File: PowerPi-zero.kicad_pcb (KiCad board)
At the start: 2 copper layers, 65 x 56 mm, 34 parts, among them J1 2444, J3 Conn_01x02, J6 Raspberry_Pi_2_3, J8 2444, Q1 30V 4A 44mΩ, Q2 50nA 150V 200mW 200mA, Q3 30V 4A 44mΩ, U1 XL4015

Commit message: Layout complete for PowerPi zero
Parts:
- removed D2: SS54, Diode_SMD:D_SMA
- removed H5, H6, H7, H8: MountingHole, MountingHole:MountingHole_3.5mm
- removed J3: Conn_01x02, Connector_JST:JST_XH_B2B-XH-A_1x02_P2.50mm_Vertical
- removed JP1: SolderJumper_3_Bridged12, Jumper:SolderJumper-3_P1.3mm_Bridged2Bar12_RoundedPad1.0x1.5mm
- moved R1 46.0 mm to (121.0, 107.1), turned to 180 degrees
- moved Q2 45.7 mm to (123.7, 106.4)
- moved R2 44.7 mm to (122.7, 100.7), turned to 0 degrees
- moved C1 44.0 mm to (104.2, 117.4), turned to 180 degrees
- moved Q3 43.9 mm to (123.6, 103.1), turned to 0 degrees
- moved R8 43.6 mm to (151.8, 115.4), turned to 180 degrees
- moved R6 42.2 mm to (151.8, 111.3), turned to 180 degrees
- moved D5 41.8 mm to (153.6, 114.6), turned to -90 degrees
- moved D3 41.0 mm to (153.6, 110.5), turned to -90 degrees
- moved H2 40.5 mm to (93.2, 97.0)
- moved H3 40.5 mm to (151.2, 97.0)
- moved J6 40.5 mm to (98.1, 98.3)
- moved J8 38.1 mm to (151.5, 102.8), turned to -90 degrees
- moved C2 37.0 mm to (111.4, 121.3), turned to -90 degrees
- moved C3 36.4 mm to (111.4, 118.1), turned to -90 degrees
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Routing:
- net VCC: track 29.0 -> 40.9 mm, vias 3 -> 0
- net Net-(D2-Pad1): track 8.10 -> 0.00 mm, vias 1 -> 0
- net +5V: track 2.95 -> 9.34 mm, vias 1 -> 0
- net Net-(D6-Pad1): track 22.4 -> 26.8 mm
- net Net-(Q2-Pad3): track 5.83 -> 7.27 mm
- net Net-(R10-Pad1): track 12.0 -> 12.7 mm
- net GND: track 4.99 -> 5.08 mm, vias 56 -> 50
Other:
- board size 65 x 56 mm -> 65 x 30 mm
- board text added: "Select one of these board edges depending upon the type of socket that is used."
- board text removed: "+"
- board text removed: "-"
- board text removed: "."
- board text removed: "12/24V"
- board text removed: "5V"
- board text removed: "AUX 5V(1A)"
- board text removed: "FAN"
- board text removed: "JLCJLCJLC"
- board text removed: "VCC"
- board text removed: "Vector 3D PowerPi Designed by Sreenivas Eadara"

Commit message: cleanup
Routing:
- net Net-(D6-Pad1): track 26.8 -> 26.1 mm
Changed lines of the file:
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@@
     (style (thickness 0.15) (arrow_length 1.27) (text_position_mode 0) (extension_height 0.58642) (extension_offset 0) keep_text_aligned)
   )
-  (segment (start 151.29 115.4) (end 151.29 115.41) (width 0.5) (layer "F.Cu") (net 1))
   (segment (start 151.29 115.41) (end 143.9 122.8) (width 0.5) (layer "F.Cu") (net 1))
   (segment (start 143.9 122.8) (end 113.45 122.8) (width 0.5) (layer "F.Cu") (net 1))
@@
   (via (at 119.8 107.1) (size 0.6) (drill 0.4) (layers "F.Cu" "B.Cu") (net 2))
   (segment (start 111.4 117.325) (end 114.9 117.325) (width 1) (layer "F.Cu") (net 3))
-  (segment (start 114.9 117.325) (end 114.925 117.3) (width 1) (layer "F.Cu") (net 3))
   (segment (start 151.280001 111.3) (end 149.5 109.519999) (width 0.5) (layer "F.Cu") (net 4))
   (segment (start 149.5 109.519999) (end 149.5 102.7) (width 0.5) (layer "F.Cu") (net 4))
-  (segment (start 153.5875 111.3) (end 153.6 111.2875) (width 0.5) (layer "F.Cu") (net 5))
   (segment (start 152.300001 111.3) (end 153.5875 111.3) (width 0.5) (layer "F.Cu") (net 5))
-  (segment (start 153.5875 115.4) (end 153.6 115.3875) (width 0.5) (layer "F.Cu") (net 6))
   (segment (start 152.31 115.4) (end 153.5875 115.4) (width 0.5) (layer "F.Cu") (net 6))
-  (segment (start 139.55 120.75) (end 139.1 120.3) (width 2) (layer "F.Cu") (net 7))
   (segment (start 128.375 119.9) (end 124.075 115.6) (width 2) (layer "F.Cu") (net 7))
   (segment (start 131.25 120.3) (end 131 120.05) (width 2) (layer "F.Cu") (net 7))
@@
   (segment (start 139.1 120.3) (end 131.25 120.3) (width 2) (layer "F.Cu") (net 7))
   (segment (start 122.75 107.05) (end 121.56 107.05) (width 0.375) (layer "F.Cu") (net 31))
-  (segment (start 121.56 107.05) (end 121.51 107.1) (width 0.375) (layer "F.Cu") (net 31))
   (segment (start 122.75 106.4) (end 124.65 106.4) (width 0.375) (layer "F.Cu") (net 31))
   (segment (start 122.75 107.05) (end 122.75 106.4) (width 0.375) (layer "F.Cu") (net 31))

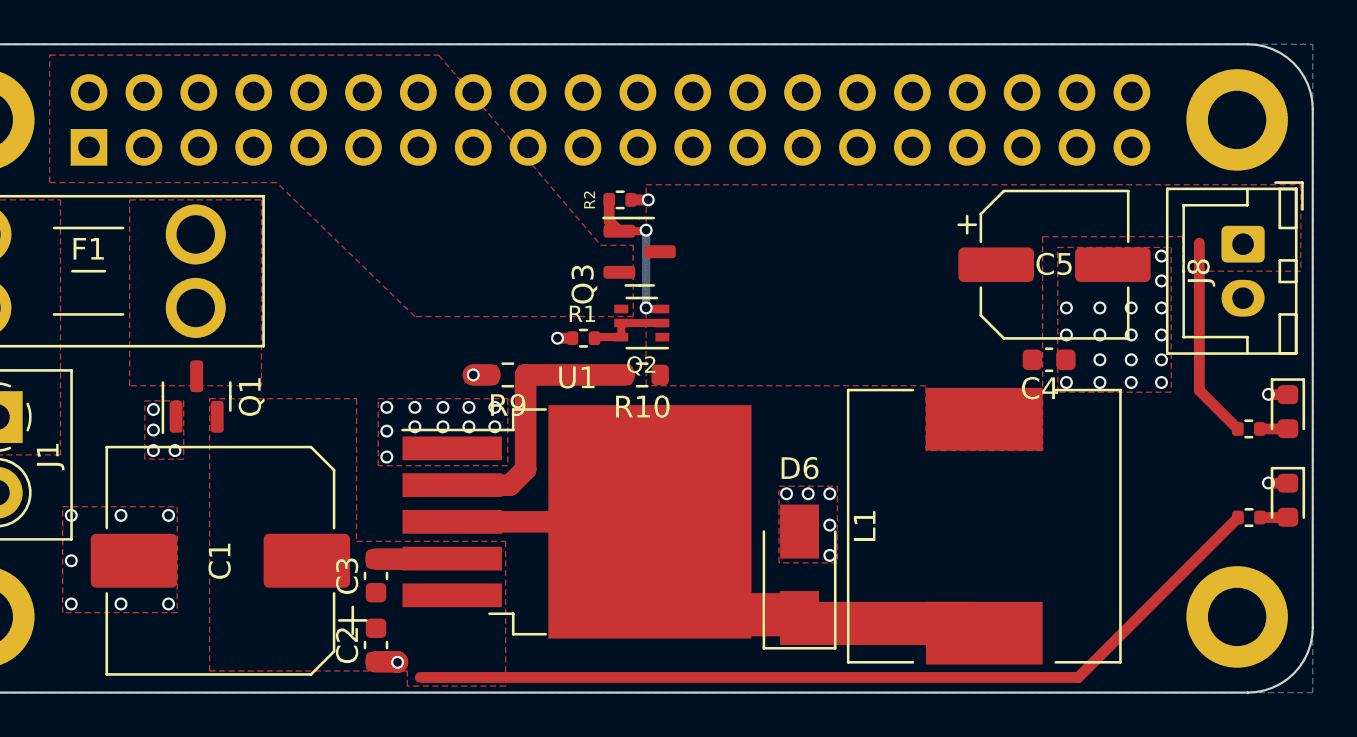
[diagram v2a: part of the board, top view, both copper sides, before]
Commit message: updated layout
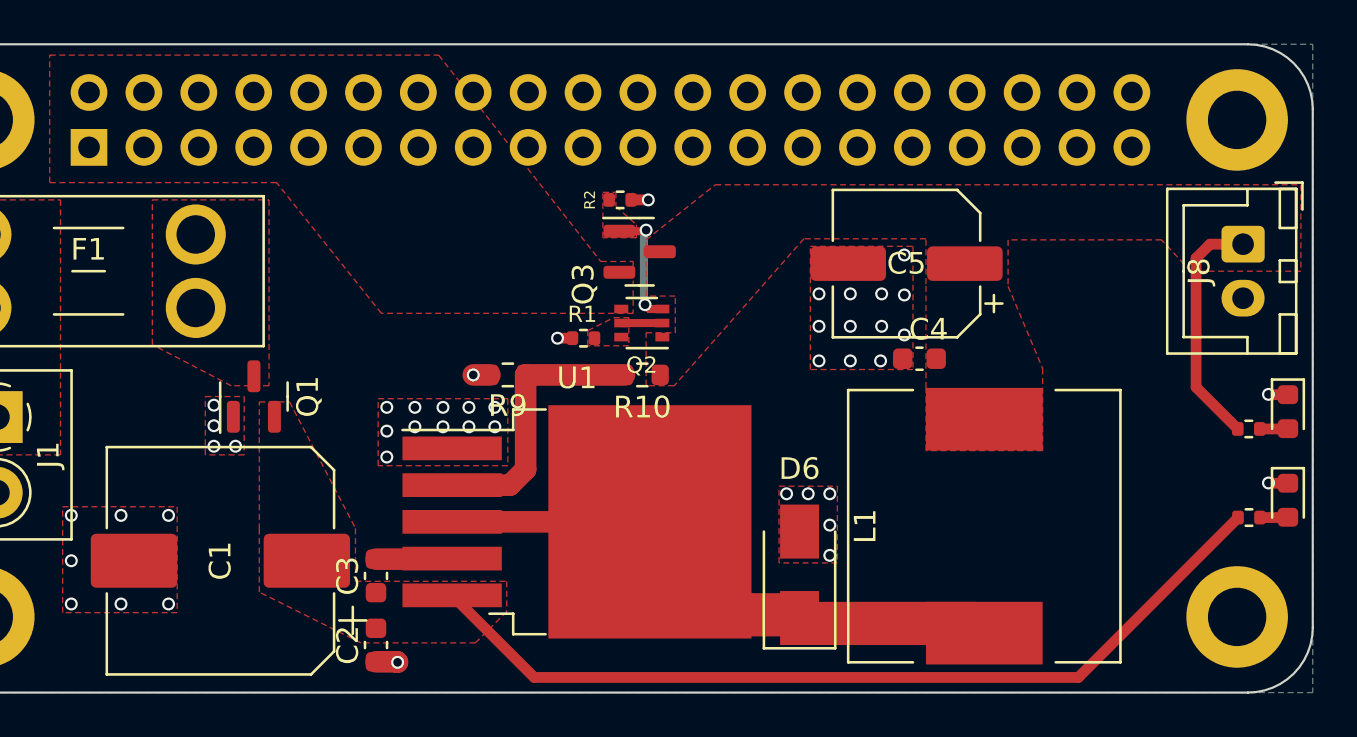
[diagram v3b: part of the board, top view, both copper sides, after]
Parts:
- moved C5 6.85 mm to (135.9, 103.7), turned to 180 degrees
- moved C4 6.00 mm to (136.6, 108.0), turned to 180 degrees
- moved Q1 2.65 mm to (105.8, 109.8)
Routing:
- net +5V: track 9.34 -> 11.2 mm
- net Net-(Q2-Pad2): track 3.74 -> 1.90 mm
- net Net-(Q2-Pad3): track 7.27 -> 5.65 mm
- net GND: vias 50 -> 45
- added copper zone on F.Cu, net Net-(Q2-Pad2)
- added copper zone on F.Cu, net Net-(Q2-Pad3)

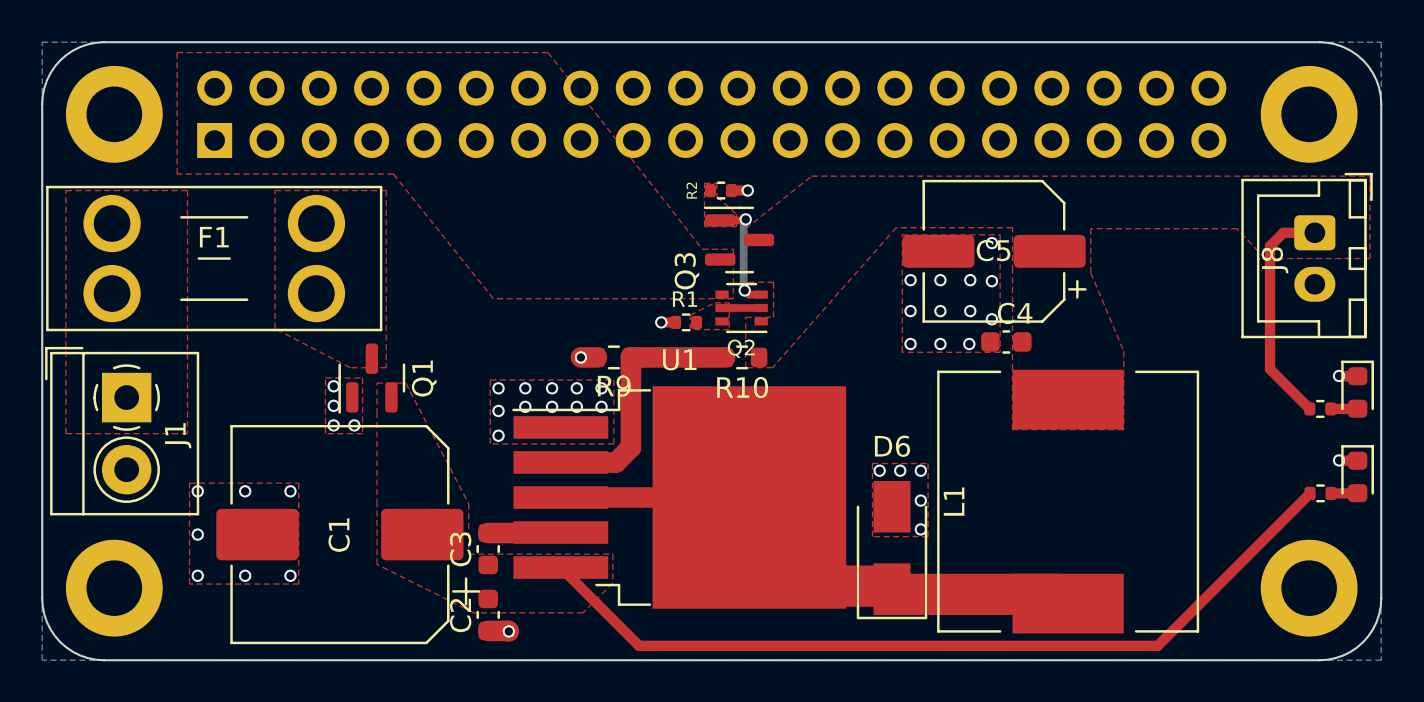
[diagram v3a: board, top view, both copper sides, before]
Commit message: updated layout and improved copper balance
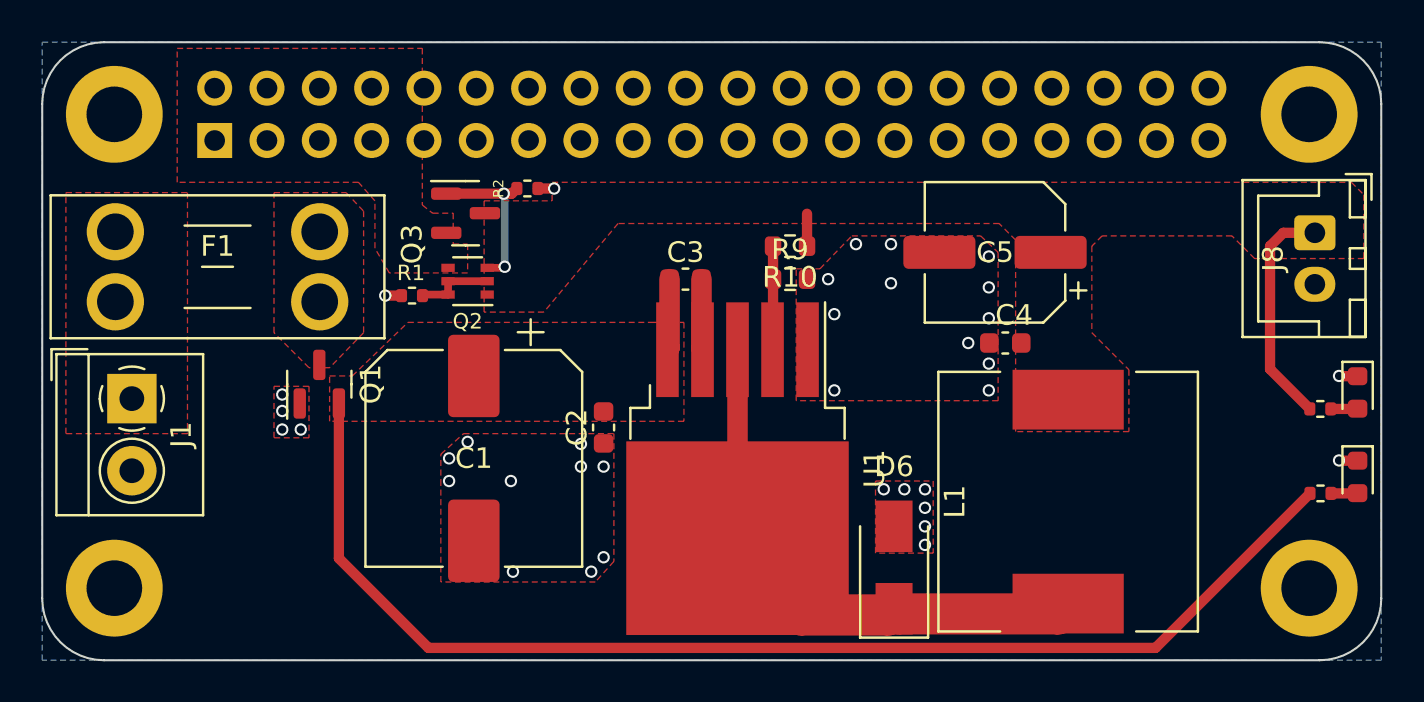
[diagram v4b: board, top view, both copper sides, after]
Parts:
- moved C3 16.2 mm to (121.0, 105.0), turned to 180 degrees
- moved Q2 13.4 mm to (110.4, 105.1)
- moved Q3 13.4 mm to (110.3, 101.8)
- moved R1 13.4 mm to (107.7, 105.8)
- moved C2 10.7 mm to (117.0, 112.2)
- moved R2 9.40 mm to (113.3, 100.6)
- moved R9 9.36 mm to (126.0, 105.0), turned to 0 degrees
- moved C1 7.48 mm to (110.7, 113.7), turned to -90 degrees
- moved R10 5.88 mm to (126.0, 103.4)
- moved U1 3.13 mm to (123.5, 114.2), turned to -90 degrees
- moved Q1 2.57 mm to (103.2, 110.1)
- moved D6 0.96 mm to (131.1, 119.0)
- moved F1 0.43 mm to (93.3, 102.7)
- moved J1 0.25 mm to (94.1, 110.8)
- moved C4 0.07 mm to (136.5, 108.1)
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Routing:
- net VCC: track 41.0 -> 63.0 mm
- net Net-(R10-Pad1): track 12.7 -> 5.04 mm
- net Net-(Q2-Pad3): track 5.65 -> 7.97 mm
- net Net-(Q2-Pad2): track 1.90 -> 3.81 mm
- net GND: track 5.08 -> 3.39 mm, vias 45 -> 36
- net +5V: track 11.2 -> 12.7 mm
- net Net-(D6-Pad1): track 26.1 -> 27.5 mm
- removed copper zone on F.Cu, net Net-(Q2-Pad2)
- removed copper zone on F.Cu, net Net-(Q2-Pad3)

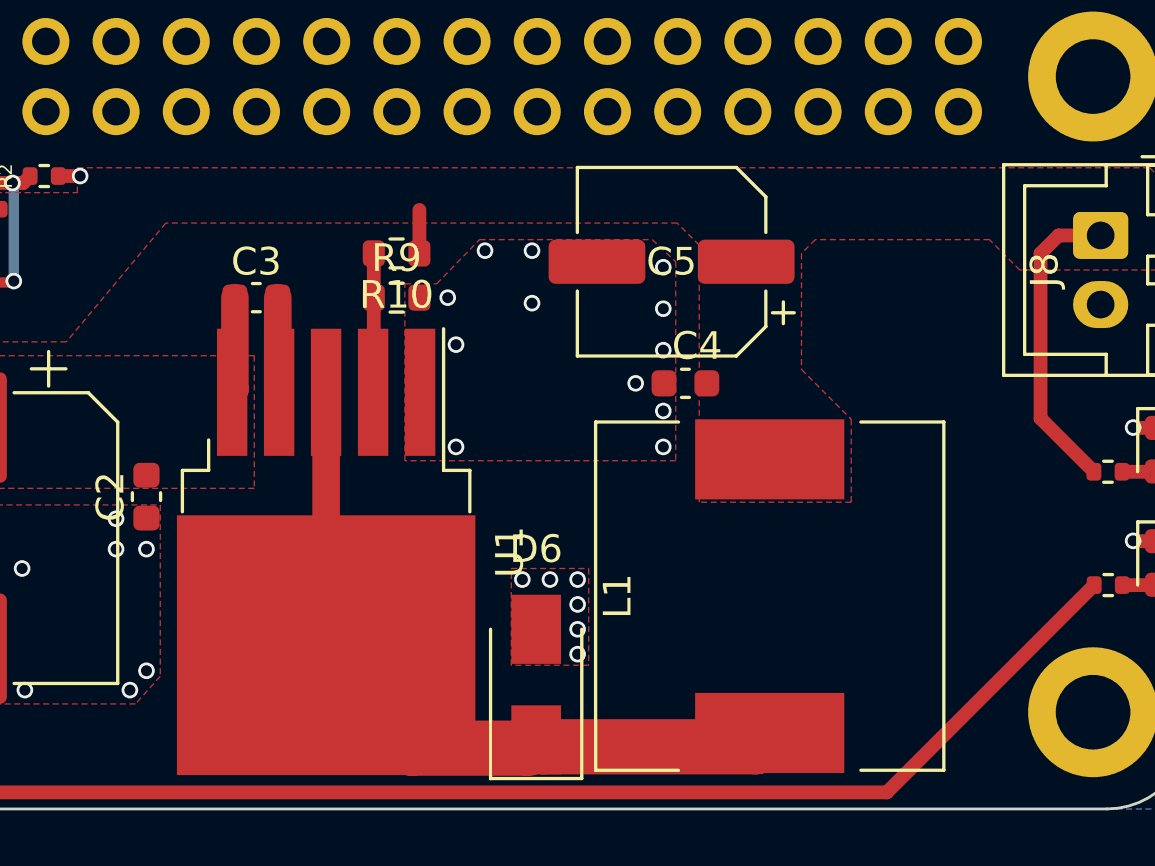
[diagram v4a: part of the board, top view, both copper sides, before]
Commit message: update to 1000 uF output electrolytic capacitor
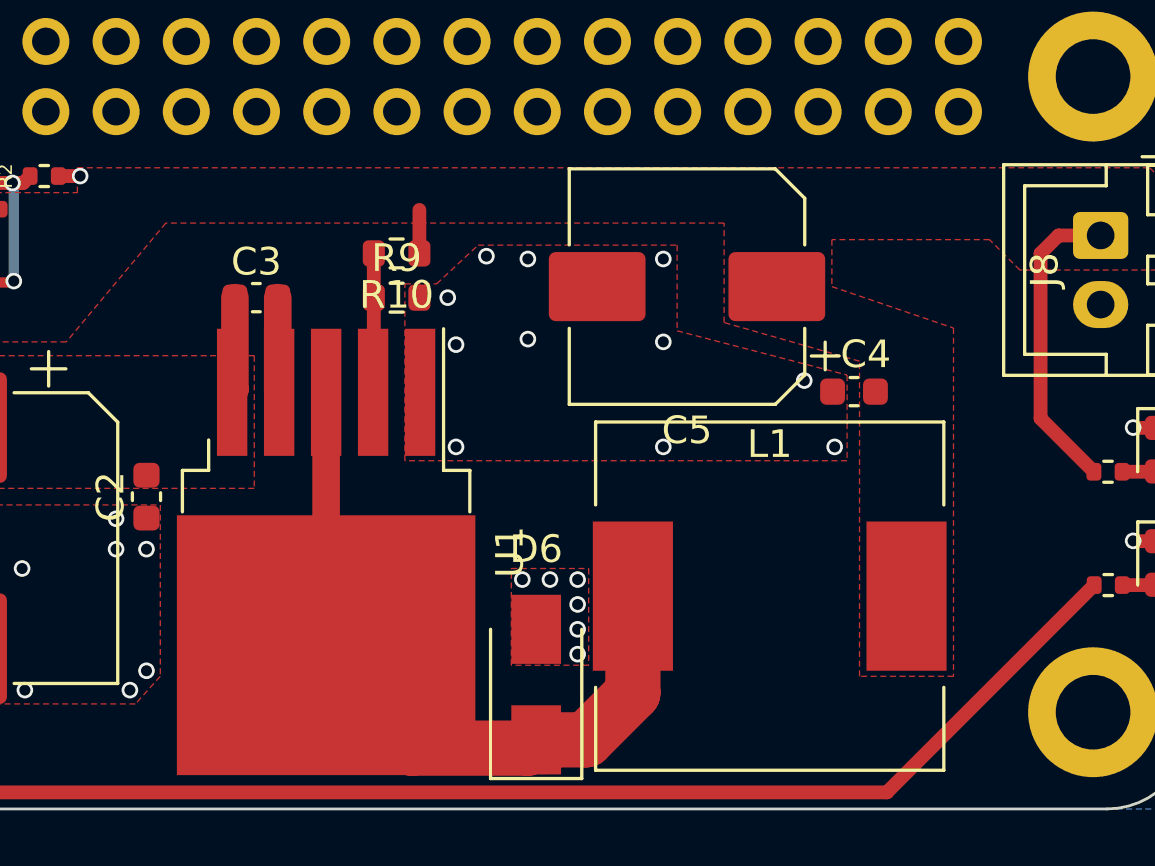
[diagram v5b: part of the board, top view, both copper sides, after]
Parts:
- C5: value 330uF -> 1000uF; footprint Capacitor_SMD:CP_Elec_6.3x7.7 -> Capacitor_SMD:CP_Elec_8x10
- moved C4 6.11 mm to (142.6, 108.4)
- moved C5 1.06 mm to (136.6, 104.6)
- turned L1 to 0 degrees
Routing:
- net Net-(D6-Pad1): track 27.5 -> 26.8 mm
- net GND: vias 36 -> 35
